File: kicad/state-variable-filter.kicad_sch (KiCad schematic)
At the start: 107 parts, among them J10 AudioJack2_SwitchT, J2 AudioJack2_SwitchT, J3 AudioJack2_SwitchT, J4 AudioJack2_SwitchT, J5 AudioJack2_SwitchT, J6 AudioJack2_SwitchT, J7 AudioJack2_SwitchT, J8 AudioJack2_SwitchT, J9 AudioJack2_SwitchT, Q1 2N3904, Q2 2N3906, Q3 2N3906, Q4 2N3906, U1 TL074, U2 TL072, U3 LM13700, U4 LM13700, U5 TL074, U6 TL072, U7 SSI2164, U8 OPA1678, U9 OPA1678

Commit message: Updating hardware design
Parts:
- removed C15: 22pF, Rumblesan_Standard_Parts:C_Rect_L7.0mm_W2.5mm_P5.00mm, symbol Rumblesan_Standard_Parts:C
- removed C18, C19, C21, C22: 100nF, Rumblesan_Standard_Parts:C_Rect_L7.0mm_W2.5mm_P5.00mm, symbol Rumblesan_Standard_Parts:C
- removed C20: 220pF, Rumblesan_Standard_Parts:C_Rect_L7.0mm_W2.5mm_P5.00mm, symbol Rumblesan_Standard_Parts:C
- removed D7: 1n4148, Rumblesan_Standard_Parts:D_DO-35_SOD27_P7.62mm_Horizontal, symbol Device:D
- removed D8: 1N4148, Rumblesan_Standard_Parts:D_DO-35_SOD27_P7.62mm_Horizontal, symbol Device:D
- removed J10: AudioJack2_SwitchT, Rumblesan_Audio_Connectors:Jack_3.5mm_QingPu_WQP-PJ398SM_Vertical, symbol Connector_Audio:AudioJack2_SwitchT
- removed Q1: 2N3904, Package_TO_SOT_THT:TO-92_Inline_Wide, symbol Transistor_BJT:2N3904
- removed Q2, Q3, Q4: 2N3906, Package_TO_SOT_THT:TO-92_Inline_Wide, symbol Transistor_BJT:2N3906
- removed R20, R25: 330r, Rumblesan_Standard_Parts:R_Axial_DIN0207_L6.3mm_D2.5mm_P10.16mm_Horizontal, symbol Device:R
- removed R26, R41, R43, R46, R47: 100k, Rumblesan_Standard_Parts:R_Axial_DIN0207_L6.3mm_D2.5mm_P10.16mm_Horizontal, symbol Rumblesan_Standard_Parts:R
- removed R27, R28: 220r, Rumblesan_Standard_Parts:R_Axial_DIN0207_L6.3mm_D2.5mm_P10.16mm_Horizontal, symbol Rumblesan_Standard_Parts:R
- removed R29, R44: 10k, Rumblesan_Standard_Parts:R_Axial_DIN0207_L6.3mm_D2.5mm_P10.16mm_Horizontal, symbol Rumblesan_Standard_Parts:R
- removed R30: 51k, Rumblesan_Standard_Parts:R_Axial_DIN0207_L6.3mm_D2.5mm_P10.16mm_Horizontal, symbol Rumblesan_Standard_Parts:R
- removed R38: 1m, Rumblesan_Standard_Parts:R_Axial_DIN0207_L6.3mm_D2.5mm_P10.16mm_Horizontal, symbol Rumblesan_Standard_Parts:R
- removed R39: 180k, Rumblesan_Standard_Parts:R_Axial_DIN0207_L6.3mm_D2.5mm_P10.16mm_Horizontal, symbol Rumblesan_Standard_Parts:R
- removed R42: 470r, Rumblesan_Standard_Parts:R_Axial_DIN0207_L6.3mm_D2.5mm_P10.16mm_Horizontal, symbol Rumblesan_Standard_Parts:R
- removed R45: 4k7, Rumblesan_Standard_Parts:R_Axial_DIN0207_L6.3mm_D2.5mm_P10.16mm_Horizontal, symbol Rumblesan_Standard_Parts:R
- removed R48: 330k, Rumblesan_Standard_Parts:R_Axial_DIN0207_L6.3mm_D2.5mm_P10.16mm_Horizontal, symbol Rumblesan_Standard_Parts:R
- removed R49: 33k, Rumblesan_Standard_Parts:R_Axial_DIN0207_L6.3mm_D2.5mm_P10.16mm_Horizontal, symbol Rumblesan_Standard_Parts:R
- removed R50: 1k, Rumblesan_Standard_Parts:R_Axial_DIN0207_L6.3mm_D2.5mm_P10.16mm_Horizontal, symbol Rumblesan_Standard_Parts:R
- removed RV8, RV9: 10k, Rumblesan_Potentiometer_THT:Potentiometer_Alpha_RD901F-40-00D_Single_Vertical, symbol Rumblesan_Standard_Parts:R_Potentiometer
- removed U1, U5: TL074, Package_DIP:DIP-14_W7.62mm_Socket, symbol Amplifier_Operational:TL074
- removed unit 3 of U2
- removed unit 1 of U2
- removed U3, U4: LM13700, Package_DIP:DIP-16_W7.62mm_Socket, symbol Amplifier_Operational:LM13700
- removed U6: TL072, Package_DIP:DIP-8_W7.62mm_Socket, symbol Amplifier_Operational:TL072
- removed U8, U9: OPA1678, symbol Amplifier_Operational:OPA1678
- added C19, C20: 10uF, Rumblesan_Standard_Parts:CP_Radial_D5.0mm_P2.00mm, symbol Device:C_Polarized
- added D10, D9: 1N4148, Rumblesan_Standard_Parts:D_DO-35_SOD27_P7.62mm_Horizontal, symbol Device:D
- added D11, D5: 1N5818, Rumblesan_Standard_Parts:D_DO-41_SOD81_P10.16mm_Horizontal, symbol Device:D_Schottky
- added D3: 1n4148, Rumblesan_Standard_Parts:D_DO-35_SOD27_P7.62mm_Horizontal, symbol Device:D
- added J1, J7: AudioJack2_SwitchT, Rumblesan_Audio_Connectors:Jack_3.5mm_QingPu_WQP-PJ398SM_Vertical, symbol Connector_Audio:AudioJack2_SwitchT
- added J12, J14: Conn_01x08_Pin, Connector_PinHeader_2.54mm:PinHeader_1x08_P2.54mm_Vertical, symbol Connector:Conn_01x08_Pin
- added J13, J2: Conn_01x08_Socket, Connector_PinSocket_2.54mm:PinSocket_1x08_P2.54mm_Vertical, symbol Connector:Conn_01x08_Socket
- added J15: Conn_02x05_Odd_Even, Rumblesan_Eurorack_Power:Eurorack_Power_IDC-Header_2x05_P2.54mm_Vertical, symbol Rumblesan_Eurorack_Power:Eurorack Power Small
- added JP1, JP2: Jumper_2_Open, Connector_PinHeader_2.54mm:PinHeader_1x02_P2.54mm_Vertical, symbol Jumper:Jumper_2_Open
- added NT1: NetTie_2, NetTie:NetTie-2_SMD_Pad0.5mm, symbol Device:NetTie_2
- added R1, R2, R4: 330r, Rumblesan_Standard_Parts:R_Axial_DIN0207_L6.3mm_D2.5mm_P10.16mm_Horizontal, symbol Device:R
- added R14, R17, R18, R25: 33k, Rumblesan_Standard_Parts:R_Axial_DIN0207_L6.3mm_D2.5mm_P10.16mm_Horizontal, symbol Rumblesan_Standard_Parts:R
- added R23: 330k, Rumblesan_Standard_Parts:R_Axial_DIN0207_L6.3mm_D2.5mm_P10.16mm_Horizontal, symbol Rumblesan_Standard_Parts:R
- added R36, R5, R6: 100k, Rumblesan_Standard_Parts:R_Axial_DIN0207_L6.3mm_D2.5mm_P10.16mm_Horizontal, symbol Rumblesan_Standard_Parts:R
- added TP1, TP2, TP3, TP4: TestPoint, Rumblesan_Standard_Parts:TestPoint_Loop_D2.50mm_Drill1.0mm_LowProfile, symbol Connector:TestPoint
- added unit 1 of U1
- added unit 3 of U1
- added U2, U4: TL074, Package_DIP:DIP-14_W7.62mm_Socket, symbol Amplifier_Operational:TL074
- C12: renamed from C5; footprint Rumblesan_Standard_Parts:C_Rect_L7.0mm_W2.5mm_P5.00mm -> Capacitor_THT:C_Rect_L7.0mm_W4.5mm_P5.00mm
- C18: renamed from C16; value 10nF -> 22pF
- C4: renamed from C6; footprint Rumblesan_Standard_Parts:C_Rect_L7.0mm_W2.5mm_P5.00mm -> Capacitor_THT:C_Rect_L7.0mm_W4.5mm_P5.00mm
- C9: renamed from C17; value 220pF -> 20pF
- R12: renamed from R37; value 330k -> 100k
- R13: renamed from R35; value 20k -> 33k
- R16: renamed from R31; value 20k -> 33k
- R30: renamed from R40; value 2k2 -> 33k
- R32: renamed from R36; value 100k -> 33k
- R33: renamed from R34; value 180k -> 100k
- R34: renamed from R32; value 100k -> 33k
- RV5: renamed from RV4; value 10k -> 10kB
- RV7: renamed from RV1; value 100r -> 2k; footprint Rumblesan_Potentiometer_THT:Potentiometer_THT_Bourns_3306P_Vertical -> Rumblesan_Potentiometer_THT:Potentiometer_Vishay_T93YB_Vertical; Spec single turn -> multi-turn
- U3: renamed from U7; footprint (none) -> Package_DIP:DIP-16_W7.62mm_Socket
- renumbered C11 to C10, C2 to C11, C9 to C13, C3 to C14, C25 to C15, C13 to C16, C23 to C17, C12 to C2, C10 to C3, C4 to C5, C8 to C6, C14 to C8, D2 to D1, D3 to D2, D6 to D4, D1 to D6, D4 to D7, D5 to D8, J8 to J10, J9 to J11, J7 to J4, J2 to J8, J4 to J9, R9 to R10, R8 to R11, R13 to R15, R3 to R19, R4 to R20, R7 to R21, R10 to R22, R16 to R24, R52 to R26, R54 to R27, R21 to R28, R12 to R29, R11 to R3, R33 to R31, R2 to R35, R1 to R7, R6 to R8, R5 to R9, RV6 to RV1, RV5 to RV2, RV7 to RV4, RV2 to RV6, U2 to U1
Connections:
- net BANDPASS_CTRL: now also J13.3 (Pin_3), R4.2
- net FILTER_INPUT_1_CTRL: now also J13.1 (Pin_1)
- net FILTER_INPUT_1_MAIN: now also J14.1 (Pin_1)
- net FILTER_INPUT_2_CTRL: now also J13.2 (Pin_2)
- net FILTER_INPUT_2_MAIN: now also J14.2 (Pin_2)
- net FREQ_ATTV_ACW_CTRL: now also J13.8 (Pin_8)
- net FREQ_ATTV_ACW_MAIN: now also J14.8 (Pin_8), U4.2 (-)
- net FREQ_ATTV_CW_CTRL: now also J13.6 (Pin_6)
- net FREQ_ATTV_CW_MAIN: now also D10.2 (A), J14.6 (Pin_6), U4.6 (-)
- net FREQ_CV_CTRL: now also J13.7 (Pin_7)
- net FREQ_CV_MAIN: now also J14.7 (Pin_7)
- net GND: now also RV3.1, U1.5 (+), U3.8 (GND), C19.2, C20.1, J1.S, J1.TN, J12.4 (Pin_4), J15.3 (GND), J15.4 (GND), J15.5 (GND), J15.6 (GND), J15.7 (GND), J15.8 (GND), J2.4 (Pin_4), J7.S, J7.TN, U1.2 (-), U2.10 (+), U2.12 (+), U2.3 (+), U2.5 (+), U4.10 (+), U4.12 (+), U4.3 (+), U4.5 (+); no longer RV3.3, U1.6 (-)
- net HIPASS_CTRL: now also J13.4 (Pin_4)
- net LOWPASS_CTRL: now also J2.3 (Pin_3), R1.2
- net PING_CTRL: now also J2.2 (Pin_2)
- net PING_MAIN: now also J12.2 (Pin_2)
- net RES_ATTV_ACW_CTRL: now also RV2.3, J2.7 (Pin_7); no longer RV2.1
- net RES_ATTV_ACW_MAIN: now also J12.7 (Pin_7), U4.13 (-)
- net RES_ATTV_CW_CTRL: now also RV2.1, J2.5 (Pin_5); no longer RV2.3
- net RES_ATTV_CW_MAIN: now also D4.2 (A), J12.5 (Pin_5), JP2.1 (A), R14.2, U4.9 (-); no longer D4.1 (K)
- net RES_CV_CTRL: now also J2.6 (Pin_6)
- net RES_CV_MAIN: now also J12.6 (Pin_6)
- net VCC: now also U3.16 (V+), C19.1, D11.1 (K), U1.8 (V+), U2.4 (V+), U4.4 (V+); no longer RV3.1, RV6.1
- net VEE: now also U3.9 (V-), C20.2, D5.2 (A), NT1.2, U1.4 (V-), U2.11 (V-), U4.11 (V-)
- net V_OCT_CTRL: now also J13.5 (Pin_5)
- net V_OCT_MAIN: now also J14.5 (Pin_5)
- net at C11.1, D6.1 (K), R10.2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: now also U1.3 (+); no longer U1.5 (+)
- net at J10.T: now also R6.2; no longer RV5.2
- net at C4.1, U3.5: now also U2.13 (-)
- net FREQ_VC: now reaches U3.6
- net FREQ_VC: now also RV7.1, RV7.2, U3.3
- net at R13.2, R16.1: now also U4.14
- net LOW_PASS_OUTPUT: now reaches C4.2, D2.1 (K), R24.1
- net LOW_PASS_OUTPUT: now also J12.3 (Pin_3), R25.2, U2.14
- net RES_VC: now reaches C9.2
- net RES_VC: now also U3.14, D3.1 (K), R14.1, TP4.1; no longer D4.2 (A)
- net at D1.1 (K), R22.2: now also TP3.1
- net at C11.2, D1.2 (A), R8.1: now also U1.1; no longer U1.7
- net HI_PASS_OUTPUT: now reaches C14.2, R21.1, R29.2
- net HI_PASS_OUTPUT: now also J14.4 (Pin_4), R18.2, U2.7; no longer R3.1
- net BAND_PASS_OUTPUT: now reaches C12.2, D8.2 (A), R11.2, R28.2
- net BAND_PASS_OUTPUT: now also J14.3 (Pin_3), JP1.2 (B), U2.1
- net at R20.1, R9.1: now also TP2.1, U2.8
- net at R9.2: now also U3.13, U2.9 (-); no longer U3.12
- net at R32.2, R34.1: now also U4.1
- net at J4.T: now also R5.2; no longer RV2.2
- net at C14.1, R19.1, R20.2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: now also R23.2, U2.6 (-)
- net at C12.1, U3.4: now also U2.2 (-)
- net at R11.1, R15.1: now also U3.15; no longer U3.10
- net at C18.2, R30.1: now also RV7.3, D9.1 (K), R36.1, TP1.1; no longer RV7.1
- net VCA_INPUT_CTRL: no longer names the net of J5.T
- net VCA_INPUT_CTRL: now also R4.1
- net VCA_OUTPUT_CTRL: no longer names the net of J6.T
- net VCA_OUTPUT_CTRL: now also R3.1
- new net: D10.1 (K), D9.2 (A), U4.7
- new net: JP2.2 (B), R36.2
- new net: D3.2 (A), D4.1 (K), U4.8
- new net: R17.2, R18.1, R25.1, U1.6 (-)
- new net: R6.1, RV5.2
- new net: J7.T, R2.1
- new net: J1.T, R1.1
- new net: JP1.1 (A), R23.1
- new net: R5.1, RV2.2
- new net +12IN: D11.2 (A), J15.10 (+12V), J15.9 (+12V)
- new net -12IN: D5.1 (K), J15.1 (-12V), J15.2 (-12V)
- new net NEG_VREF_CTRL: J2.8 (Pin_8), RV3.3, RV6.1
- new net NEG_VREF_MAIN: J12.8 (Pin_8), NT1.1
- new net NOTCH_CTRL: J2.1 (Pin_1), R2.2
- new net NOTCH_OUTPUT: J12.1 (Pin_1), R17.1, U1.7
- no-connect marks 9 -> 4
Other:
- note removed: "If volt per octave tuning is important then R40 should ideally be a 2K +3300ppm/°C tempco resistor"
- note removed: "TODO calculate these values"
- note removed: "Vout = Vin * (220 / 100k + 220) * 19.2 * i_vca * 51k Gain = Vout/Vin Gain = 1.07"
- note removed: "i_vca ma = Vc/Rin * (1k + 33k)/1k 5V input so 5v/330 * 34 = 0.51ma"
- moved on the sheet: C1, C10, C11, C12, C13, C14, C15, C16, C17, C18, C2, C3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

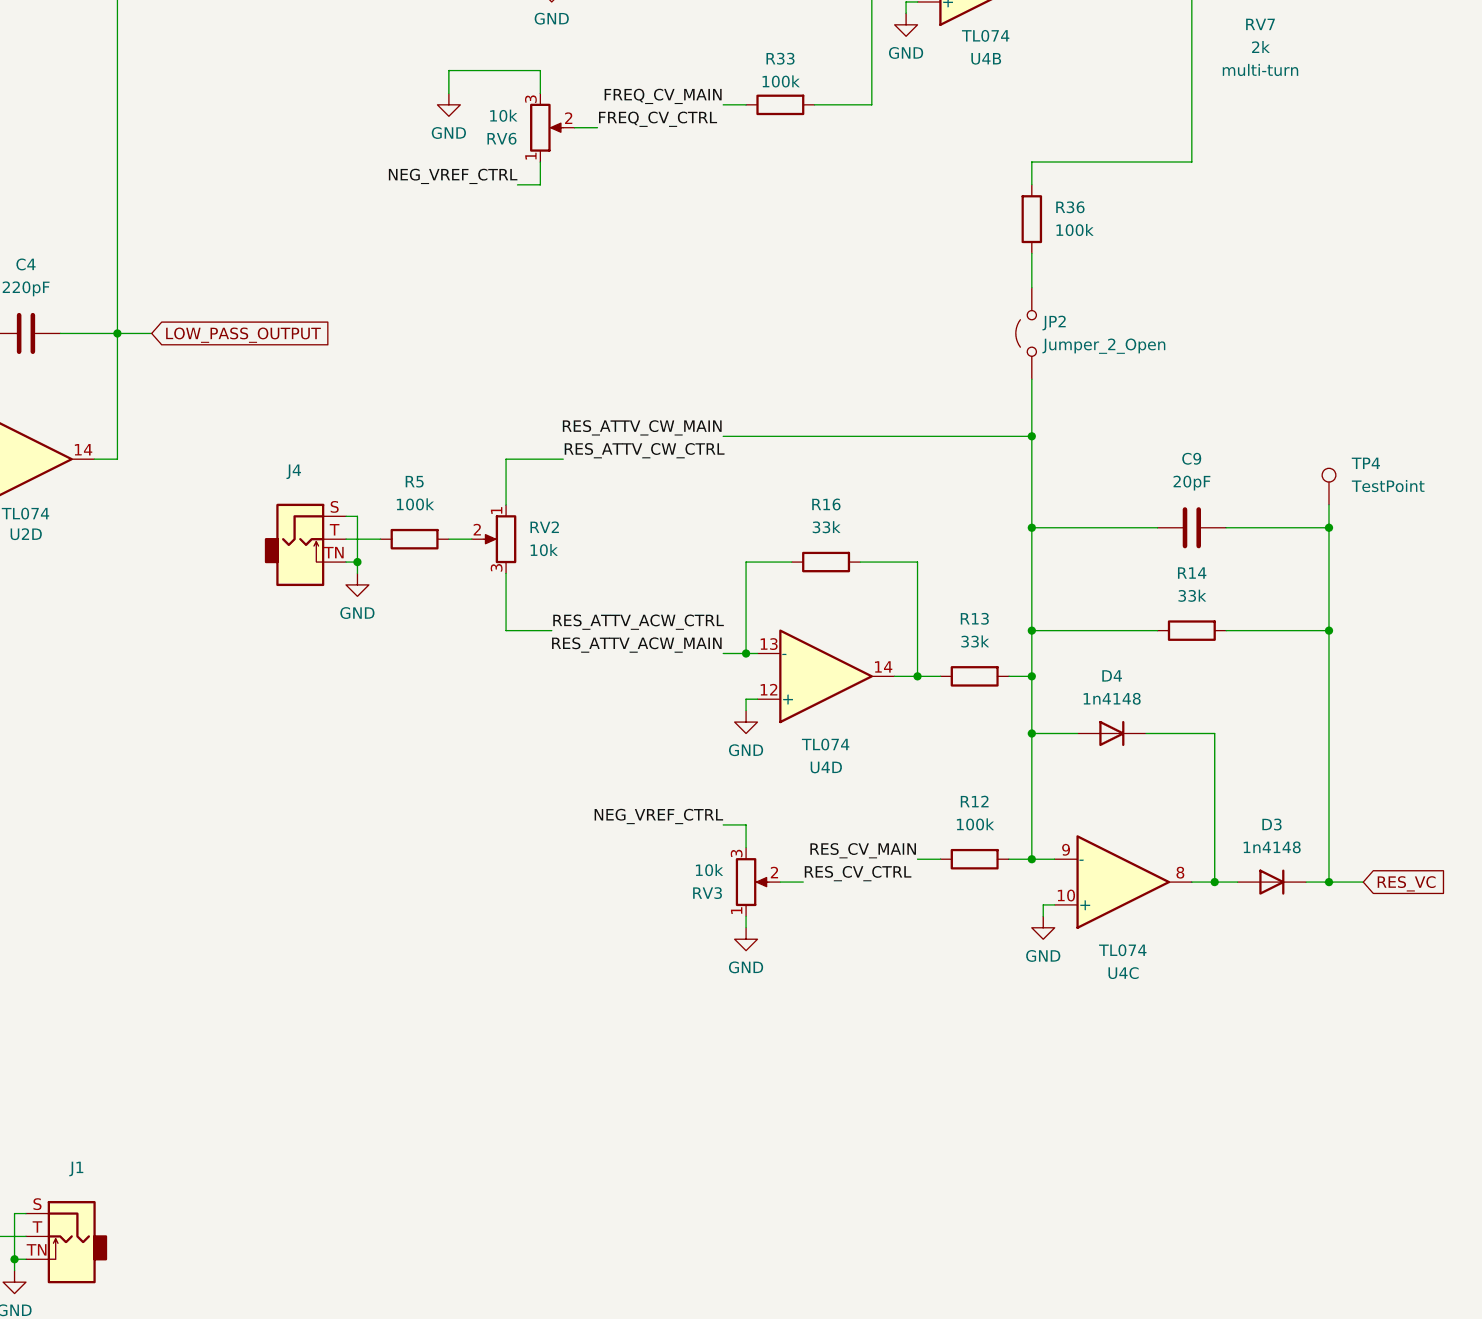
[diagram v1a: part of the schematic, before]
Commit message: Updating design
* Adding resonance control curve jumper
* improving layout
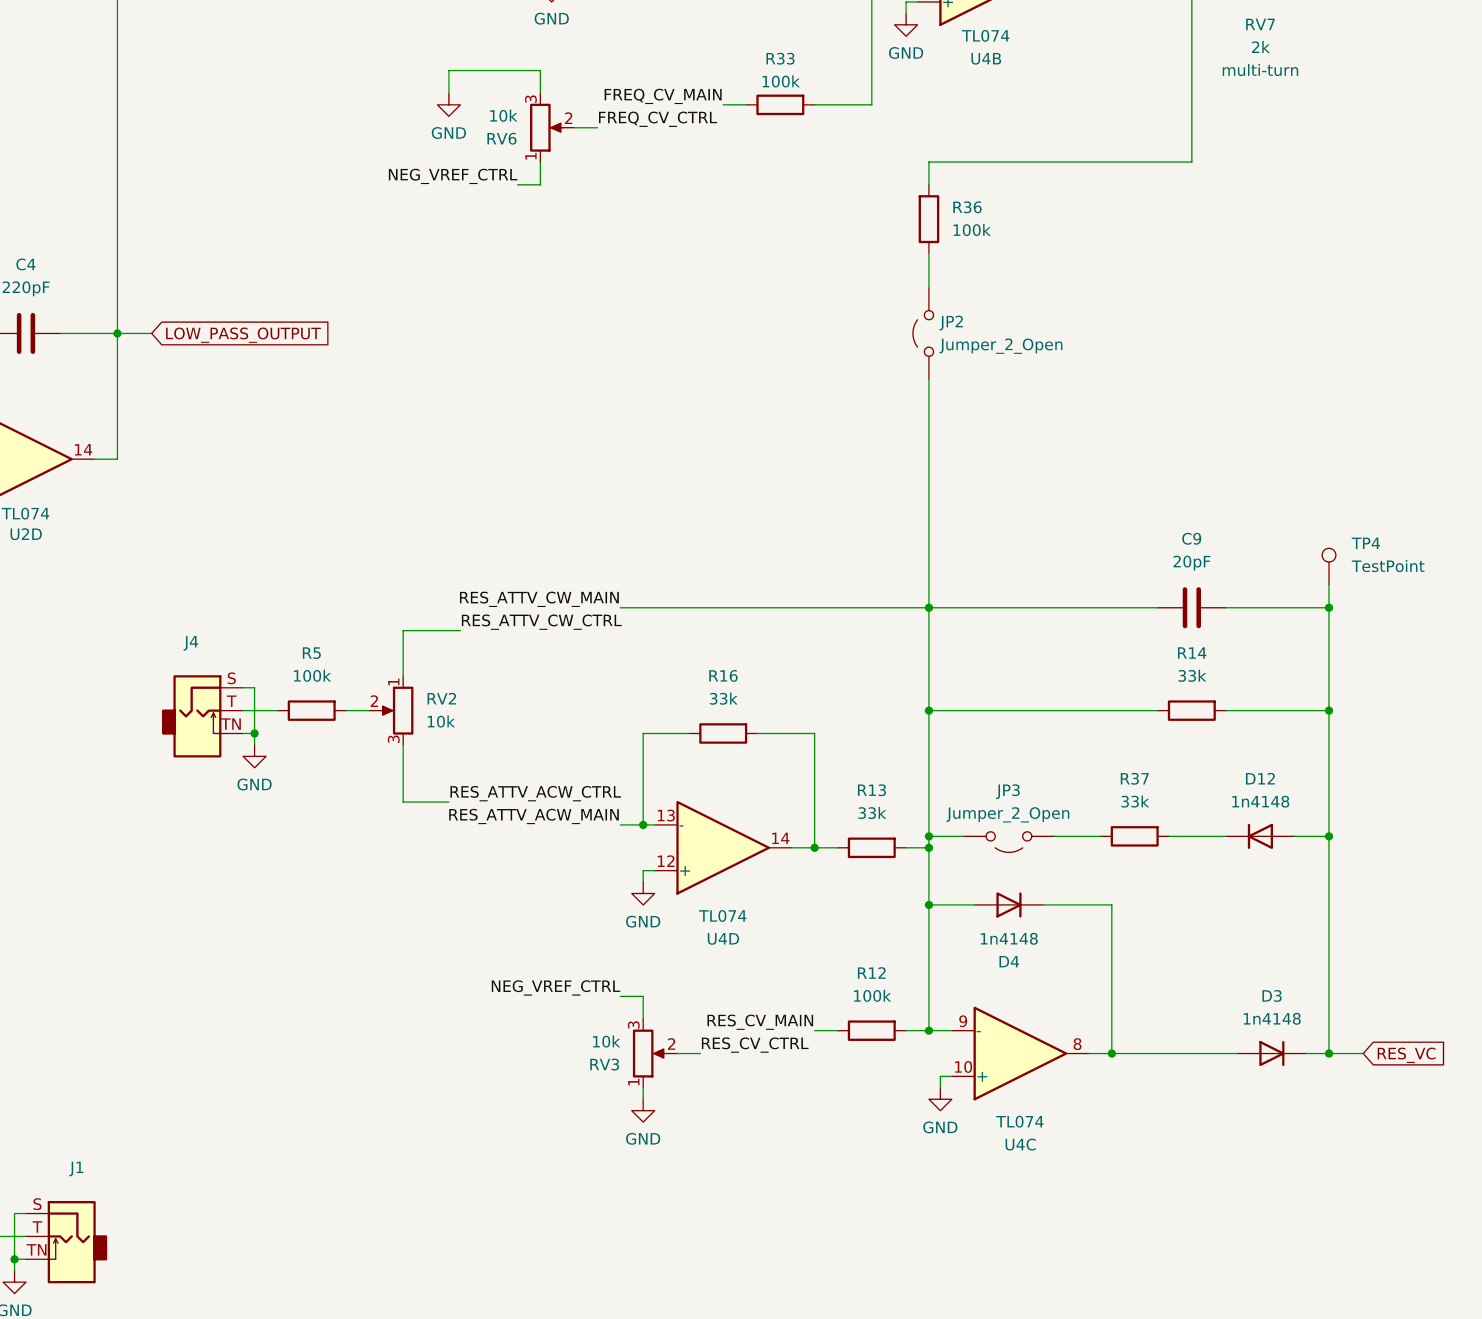
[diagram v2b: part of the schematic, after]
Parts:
- added D12: 1n4148, Rumblesan_Standard_Parts:D_DO-35_SOD27_P7.62mm_Horizontal, symbol Device:D
- added JP3: Jumper_2_Open, Connector_PinHeader_2.54mm:PinHeader_1x02_P2.54mm_Vertical, symbol Jumper:Jumper_2_Open
- added R37: 33k, Rumblesan_Standard_Parts:R_Axial_DIN0207_L6.3mm_D2.5mm_P10.16mm_Horizontal, symbol Rumblesan_Standard_Parts:R
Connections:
- net RES_ATTV_CW_MAIN: now also JP3.2 (B)
- net RES_VC: now also D12.2 (A)
- new net: D12.1 (K), R37.1
- new net: JP3.1 (A), R37.2
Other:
- moved on the sheet: C9, D3, D4, J4, JP2, R12, R13, R14, R16, R36, R5, RV2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

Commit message: Fixing a couple issues with schematic and layout
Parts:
- added H1, H2, H3, H4: MountingHole_Pad, Rumblesan_Standard_Parts:MountingHole_3.2mm_M3_DIN965_Pad, symbol Mechanical:MountingHole_Pad
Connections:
- net GND: now also H1.1, H2.1, H3.1, H4.1

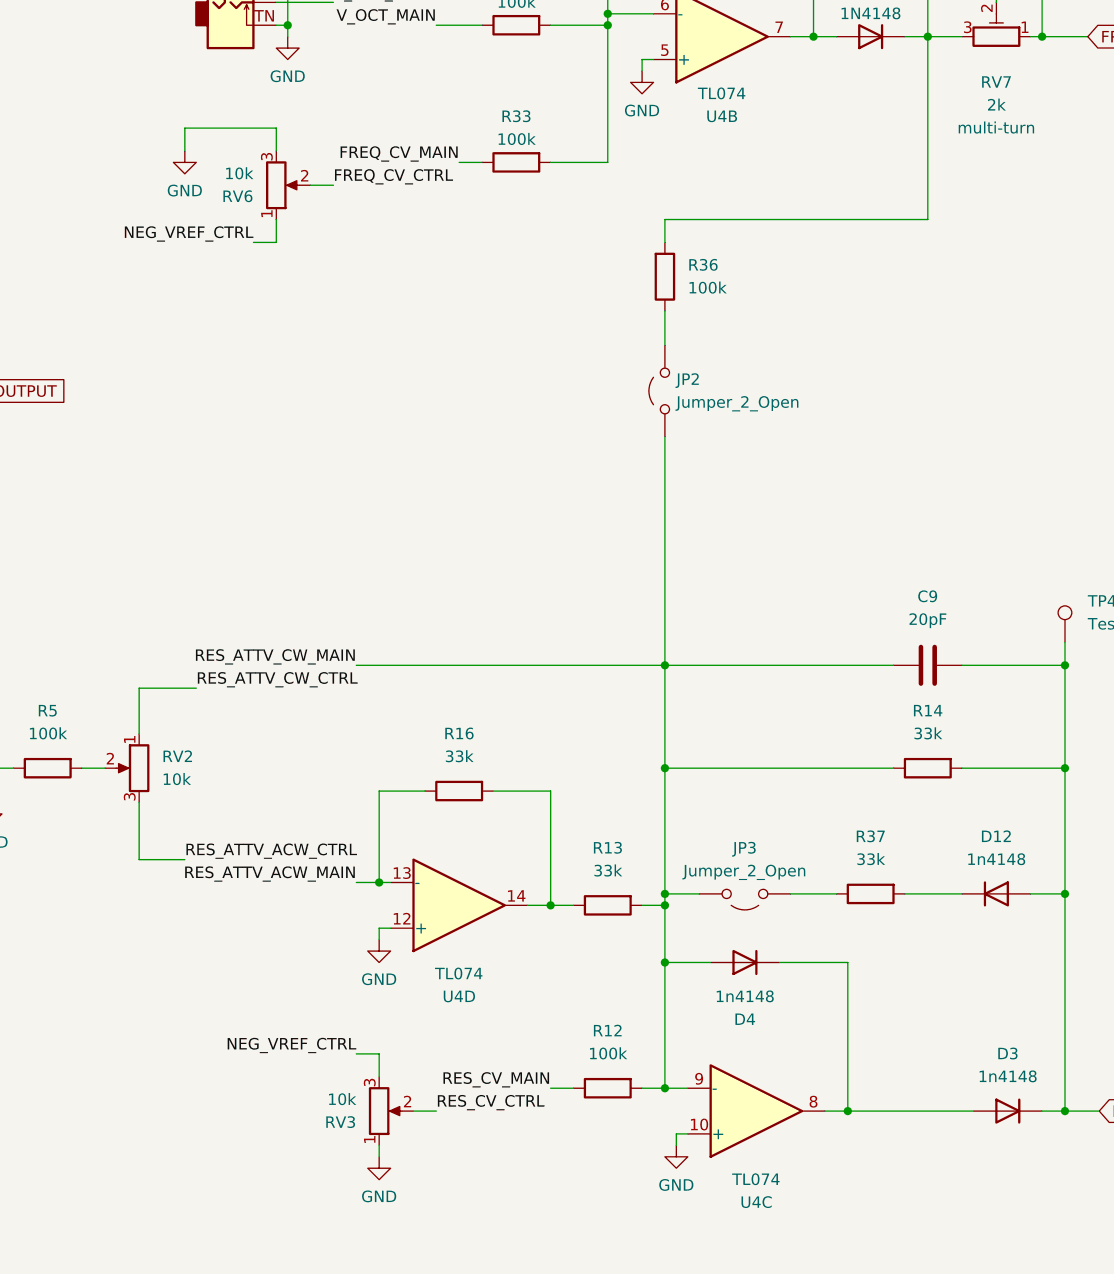
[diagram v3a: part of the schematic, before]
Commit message: Fixing minor BOM value issues
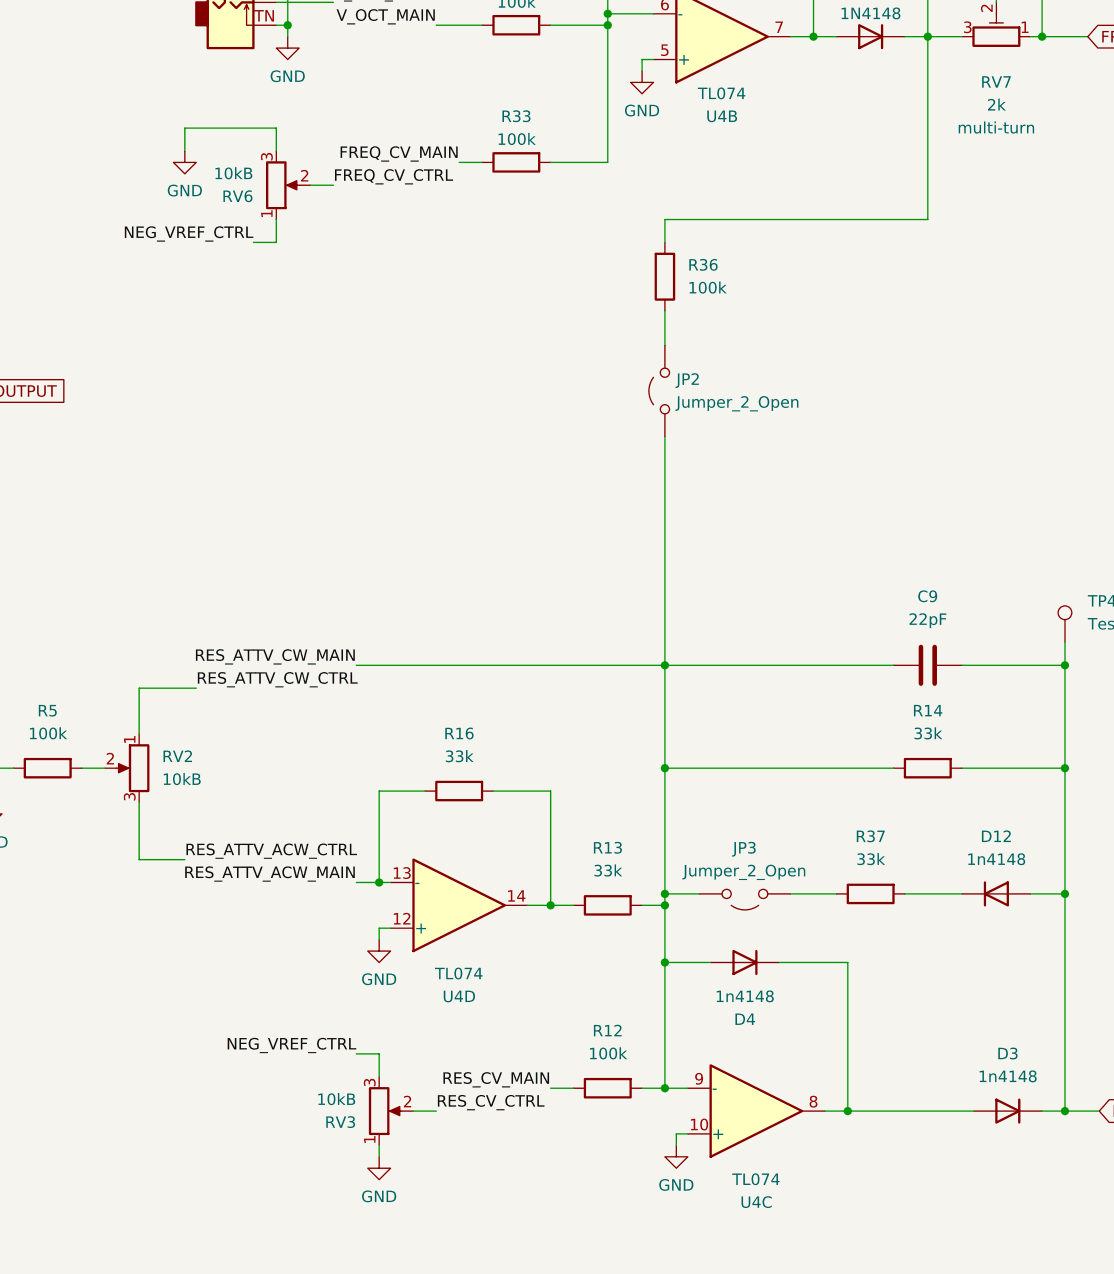
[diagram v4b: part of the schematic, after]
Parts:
- C9: value 20pF -> 22pF
- RV2, RV3, RV6: value 10k -> 10kB
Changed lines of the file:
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@@
 			)
 		)
-		(property "Value" "10k"
+		(property "Value" "10kB"
 			(at 312.42 180.3401 0)
 			(effects
@@
 			)
 		)
-		(property "Value" "20pF"
+		(property "Value" "22pF"
 			(at 375.92 127 90)
 			(effects
@@
 			)
 		)
-		(property "Value" "10k"
+		(property "Value" "10kB"
 			(at 300.99 77.4701 0)
 			(effects
@@
 			)
 		)
-		(property "Value" "10k"
+		(property "Value" "10kB"
 			(at 290.83 144.7799 0)
 			(effects

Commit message: Updating schematic after value tweaks
and regenerating BOMs
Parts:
- C1: Spec ceramic C0G -> ceramic X7R
- C19, C20: Spec (none) -> aluminium electrolytic
- D12: value 1n4148 -> 1N4148; now not fitted
- D3, D4: value 1n4148 -> 1N4148
- JP1, JP2, JP3, R23, R36, R37: now not fitted
- R12: value 100k -> 270k
- R33: value 100k -> 150k
- R7: value 180k -> 100k
- R8: value 1M5 -> 1m5
- TP1, TP2, TP3, TP4: now left out of the parts list
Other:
- moved on the sheet: C11, R8
